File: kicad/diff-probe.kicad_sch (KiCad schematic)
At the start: 39 parts, among them IC3 LMH6702, IC4 LMH6702, IC5 LMH6702, J3 HEADER-1X2CARD-EDGE, J4 CON-1X3-TAB-AMP-29173-3-NARROW, X2 SMA--BU-SMA-H

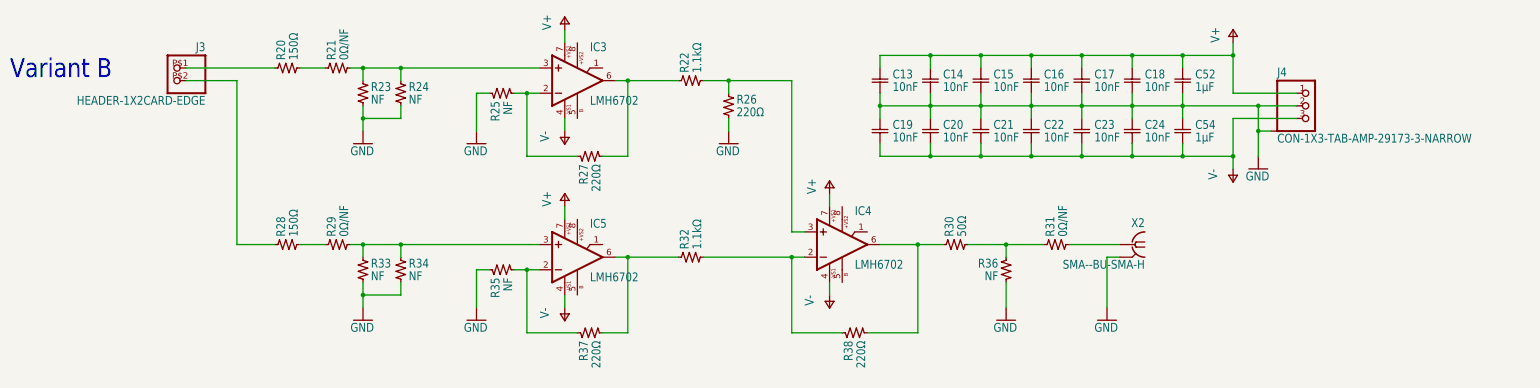
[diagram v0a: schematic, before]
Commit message: Remove NF resistors and add LCSC part numbers
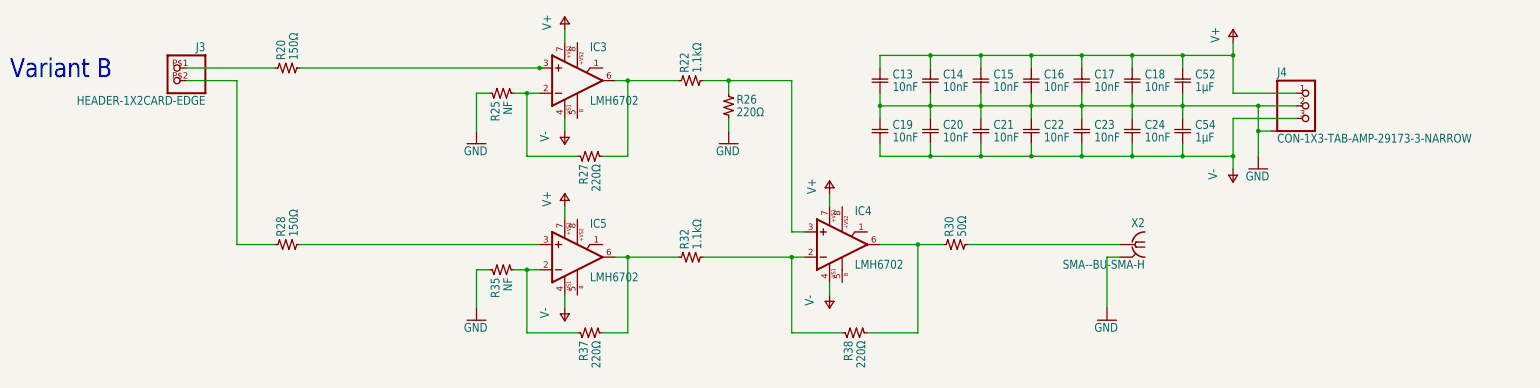
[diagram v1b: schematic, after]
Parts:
- removed R21, R29, R31: 0Ω/NF, 0402-SQUARE, symbol diff-probe-eagle-import:R-US-0402-SQUARE
- removed R23, R24, R33, R34, R36: NF, 0402-SQUARE, symbol diff-probe-eagle-import:R-US-0402-SQUARE
- C13, C14, C15, C16, C17, C18, C19, C20, C21, C22, C23, C24: LCSC (none) -> C15195
- C52, C54: LCSC (none) -> C52923
- R20, R28: LCSC (none) -> C25082
- R22, R32: LCSC (none) -> C25860
- R26, R27, R37, R38: LCSC (none) -> C25091
- R30: LCSC (none) -> C477760
- X2: LCSC (none) -> C1509224
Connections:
- net at R30.P$2 (2): now also X2.1
- net at R28.P$2 (2): now also IC5.3 (+IN)
- net at R20.P$2 (2): now also IC3.3 (+IN)

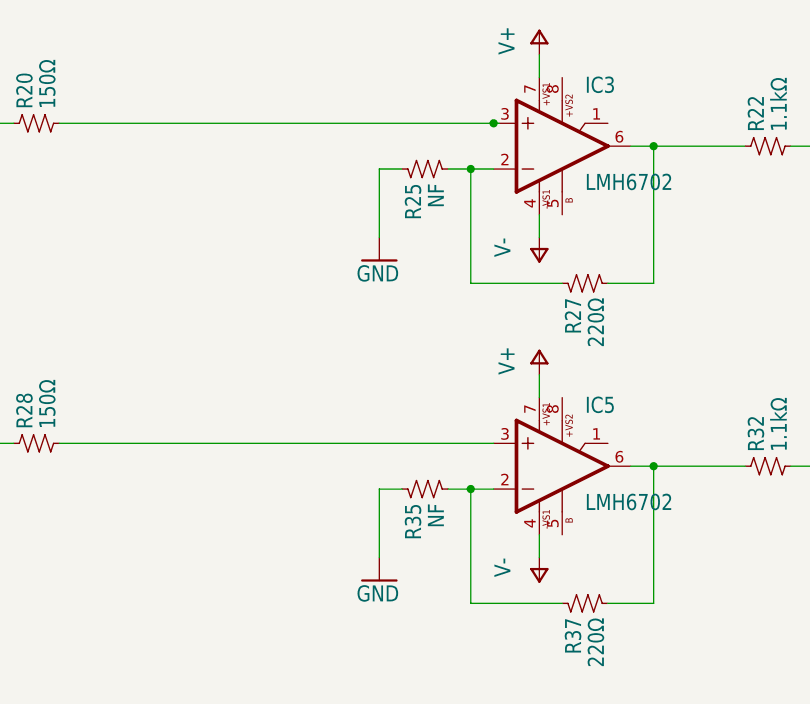
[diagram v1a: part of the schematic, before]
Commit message: remove NF resistors and rotate input resistors
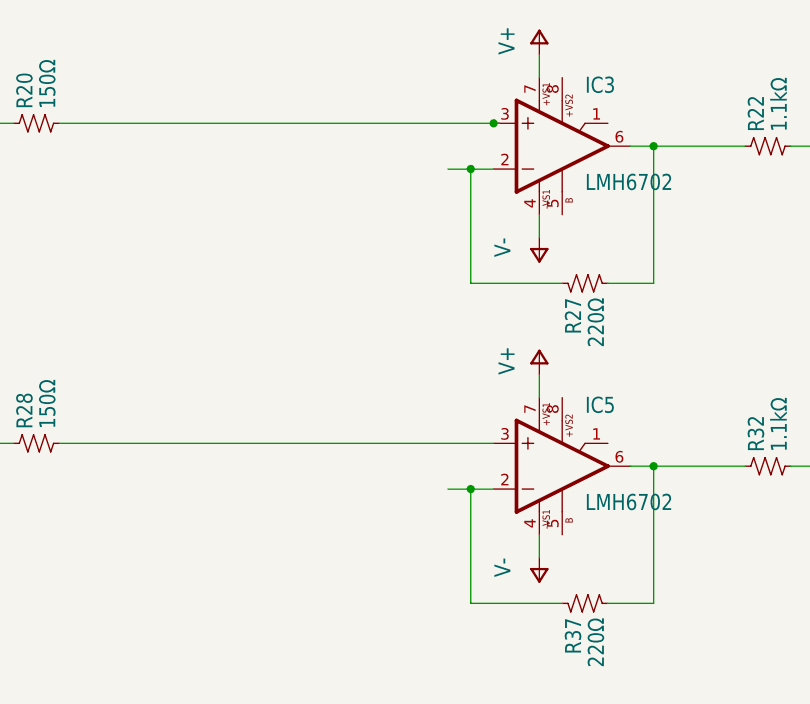
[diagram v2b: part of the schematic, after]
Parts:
- removed R25, R35: NF, 0402-SQUARE, symbol diff-probe-eagle-import:R-US-0402-SQUARE
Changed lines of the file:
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@@
   (junction (at 213.36 86.36) (diameter 0) (color 0 0 0 0)
   )
-  (wire (pts (xy 111.76 109.22) (xy 114.3 109.22))
-    (stroke (width 0) (type default) (color 0 0 0 0))
-  )
   (wire (pts (xy 203.2 76.2) (xy 203.2 73.66))
     (stroke (width 0) (type default) (color 0 0 0 0))
@@
     (stroke (width 0) (type default) (color 0 0 0 0))
   )
-  (wire (pts (xy 114.3 73.66) (xy 111.76 73.66))
-    (stroke (width 0) (type default) (color 0 0 0 0))
-  )
   (wire (pts (xy 142.24 121.92) (xy 142.24 106.68))
     (stroke (width 0) (type default) (color 0 0 0 0))
@@
     (stroke (width 0) (type default) (color 0 0 0 0))
   )
-  (wire (pts (xy 111.76 116.84) (xy 111.76 109.22))
-    (stroke (width 0) (type default) (color 0 0 0 0))
-  )
   (wire (pts (xy 175.26 101.6) (xy 175.26 71.12))
     (stroke (width 0) (type default) (color 0 0 0 0))
@@
   )
   (wire (pts (xy 213.36 76.2) (xy 213.36 73.66))
-    (stroke (width 0) (type default) (color 0 0 0 0))
-  )
-  (wire (pts (xy 111.76 73.66) (xy 111.76 81.28))
     (stroke (width 0) (type default) (color 0 0 0 0))
   )
@@
     (pin "P$2")
   )
-  (symbol (lib_id "diff-probe-eagle-import:GND") (at 111.76 83.82 0) (unit 1)
-    (in_bom yes) (on_board yes)
-    (property "Reference" "#GND010" (id 0) (at 111.76 83.82 0)
-      (effects (font (size 1.27 1.27)) hide)
-    )
-    (property "Value" "GND" (id 1) (at 109.22 86.36 0)
-      (effects (font (size 1.778 1.5113)) (justify left bottom))
-    )
-    (property "Footprint" "" (id 2) (at 111.76 83.82 0)
-      (effects (font (size 1.27 1.27)) hide)
-    )
-    (property "Datasheet" "" (id 3) (at 111.76 83.82 0)
-      (effects (font (size 1.27 1.27)) hide)
-    )
-    (pin "1")
-  )
   (symbol (lib_id "diff-probe-eagle-import:C-EU-0402-SQUARE") (at 193.04 71.12 0) (unit 1)
     (in_bom yes) (on_board yes)
@@
     )
     (property "Datasheet" "" (id 3) (at 53.34 66.04 0)
-      (effects (font (size 1.27 1.27)) hide)
-    )
-    (pin "P$1")
-    (pin "P$2")
-  )
-  (symbol (lib_id "diff-probe-eagle-import:R-US-0402-SQUARE") (at 116.84 73.66 90) (mirror x) (unit 1)
-    (in_bom yes) (on_board yes)
-    (property "Reference" "R25" (id 0) (at 115.57 75.2475 0)
-      (effects (font (size 1.778 1.5113)) (justify left))
-    )
-    (property "Value" "NF" (id 1) (at 118.11 75.2475 0)
-      (effects (font (size 1.778 1.5113)) (justify left))
-    )
-    (property "Footprint" "0402-SQUARE" (id 2) (at 116.84 73.66 0)
-      (effects (font (size 1.27 1.27)) hide)
-    )
-    (property "Datasheet" "" (id 3) (at 116.84 73.66 0)
       (effects (font (size 1.27 1.27)) hide)
     )
@@
     (pin "P$2")
   )
-  (symbol (lib_id "diff-probe-eagle-import:R-US-0402-SQUARE") (at 116.84 109.22 90) (mirror x) (unit 1)
-    (in_bom yes) (on_board yes)
-    (property "Reference" "R35" (id 0) (at 115.57 110.8075 0)
-      (effects (font (size 1.778 1.5113)) (justify left))
-    )
-    (property "Value" "NF" (id 1) (at 118.11 110.8075 0)
-      (effects (font (size 1.778 1.5113)) (justify left))
-    )
-    (property "Footprint" "0402-SQUARE" (id 2) (at 116.84 109.22 0)
-      (effects (font (size 1.27 1.27)) hide)
-    )
-    (property "Datasheet" "" (id 3) (at 116.84 109.22 0)
-      (effects (font (size 1.27 1.27)) hide)
-    )
-    (pin "P$1")
-    (pin "P$2")
-  )
   (symbol (lib_id "diff-probe-eagle-import:GND") (at 238.76 119.38 0) (unit 1)
     (in_bom yes) (on_board yes)
@@
     (pin "8")
   )
-  (symbol (lib_id "diff-probe-eagle-import:GND") (at 111.76 119.38 0) (unit 1)
-    (in_bom yes) (on_board yes)
-    (property "Reference" "#GND014" (id 0) (at 111.76 119.38 0)
-      (effects (font (size 1.27 1.27)) hide)
-    )
-    (property "Value" "GND" (id 1) (at 109.22 121.92 0)
-      (effects (font (size 1.778 1.5113)) (justify left bottom))
-    )
-    (property "Footprint" "" (id 2) (at 111.76 119.38 0)
-      (effects (font (size 1.27 1.27)) hide)
-    )
-    (property "Datasheet" "" (id 3) (at 111.76 119.38 0)
-      (effects (font (size 1.27 1.27)) hide)
-    )
-    (pin "1")
-  )
   (symbol (lib_id "diff-probe-eagle-import:C-EU-0402-SQUARE") (at 223.52 81.28 0) (unit 1)
     (in_bom yes) (on_board yes)
@@
   )
   (symbol_instances
-    (path "/5684e95c-6824-46cf-8e72-881178a51d31"
-      (reference "#GND010") (unit 1) (value "GND") (footprint "")
-    )
     (path "/7684f860-395c-40b3-8cc0-a644dcdbc220"
       (reference "#GND011") (unit 1) (value "GND") (footprint "")
@@
       (reference "#GND012") (unit 1) (value "GND") (footprint "")
     )
-    (path "/cad44c02-7fd2-4e9a-b93a-e1b73d6a3ee6"
-      (reference "#GND014") (unit 1) (value "GND") (footprint "")
-    )
     (path "/bab3431c-ede6-417b-8033-763748a11a9f"
       (reference "#GND016") (unit 1) (value "GND") (footprint "")
@@
       (reference "R22") (unit 1) (value "1.1kΩ") (footprint "0402-SQUARE")
     )
-    (path "/5c9202d7-6a93-43b3-87c0-77347fd72885"
-      (reference "R25") (unit 1) (value "NF") (footprint "0402-SQUARE")
-    )
     (path "/9b315454-a4a0-4952-bdbe-d4a8e96c16f9"
       (reference "R26") (unit 1) (value "220Ω") (footprint "0402-SQUARE")
@@
       (reference "R32") (unit 1) (value "1.1kΩ") (footprint "0402-SQUARE")
     )
-    (path "/baaf14d0-0c5c-4bf0-82d7-5ee71082500d"
-      (reference "R35") (unit 1) (value "NF") (footprint "0402-SQUARE")
-    )
     (path "/f0e6fae4-0008-43ed-8719-bf62839f601f"

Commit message: use a better SMA connector
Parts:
- X2: LCSC C1509224 -> C1509230
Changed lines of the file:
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@@
       (effects (font (size 1.27 1.27)) hide)
     )
-    (property "LCSC" "C1509224" (id 4) (at 243.84 104.14 0)
+    (property "LCSC" "C1509230" (id 4) (at 243.84 104.14 0)
       (effects (font (size 1.27 1.27)) hide)
     )
